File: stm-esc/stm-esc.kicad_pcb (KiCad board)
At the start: 2 copper layers, 57 x 48 mm, 39 parts, among them J1 RCP, J10 COUT, J2 Conn_01x06, J3 USART, J4 Conn_01x06, J5 SWIM, J6 AOUT, J7 CONN_01X01, J8 CONN_01X01, J9 BOUT, Q1 FDMS86350, Q2 FDMS86350, Q3 FDMS86350, Q4 FDMS86350, Q5 FDMS86350, Q6 FDMS86350, U2 APE8865N-33-HF-3, U3 stm32f051xx-lqfp32, U4 IR2103, U5 IR2103, U6 IR2103

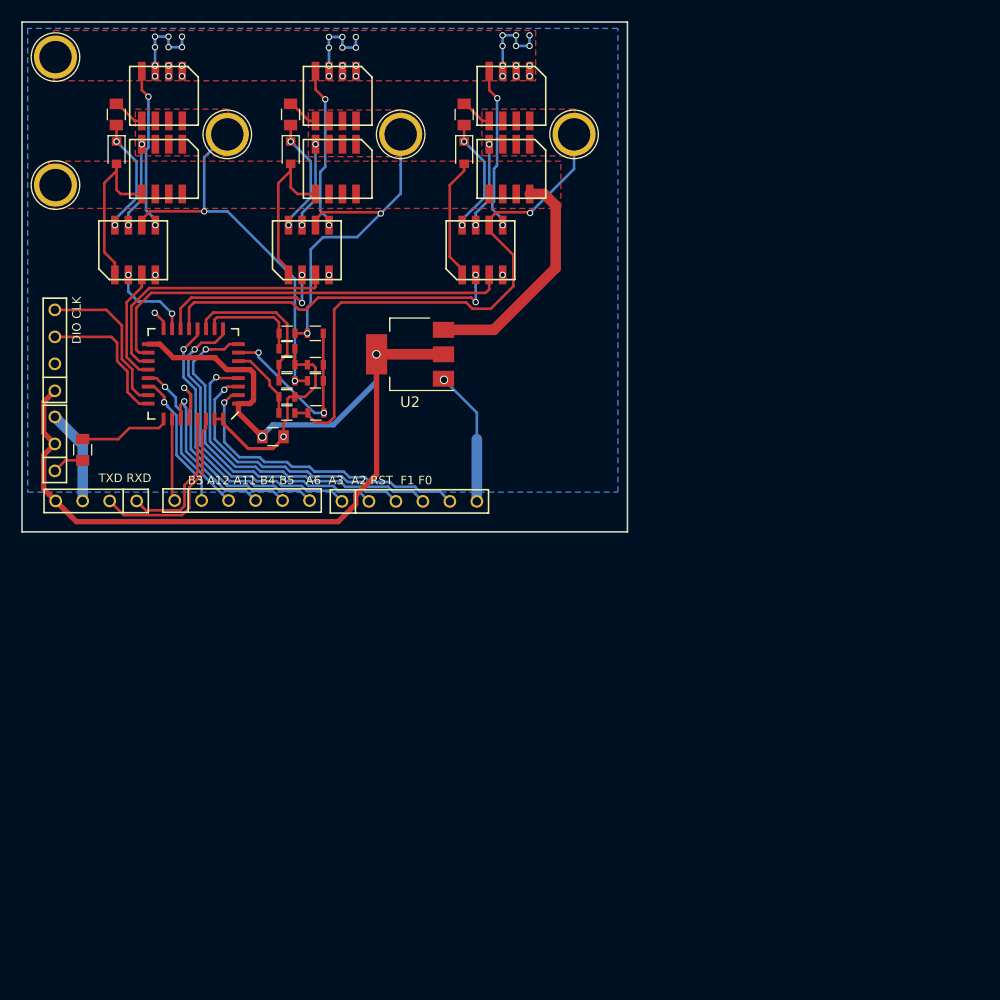
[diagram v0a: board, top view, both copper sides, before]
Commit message: stm-esc 48pin mcu 定板打样
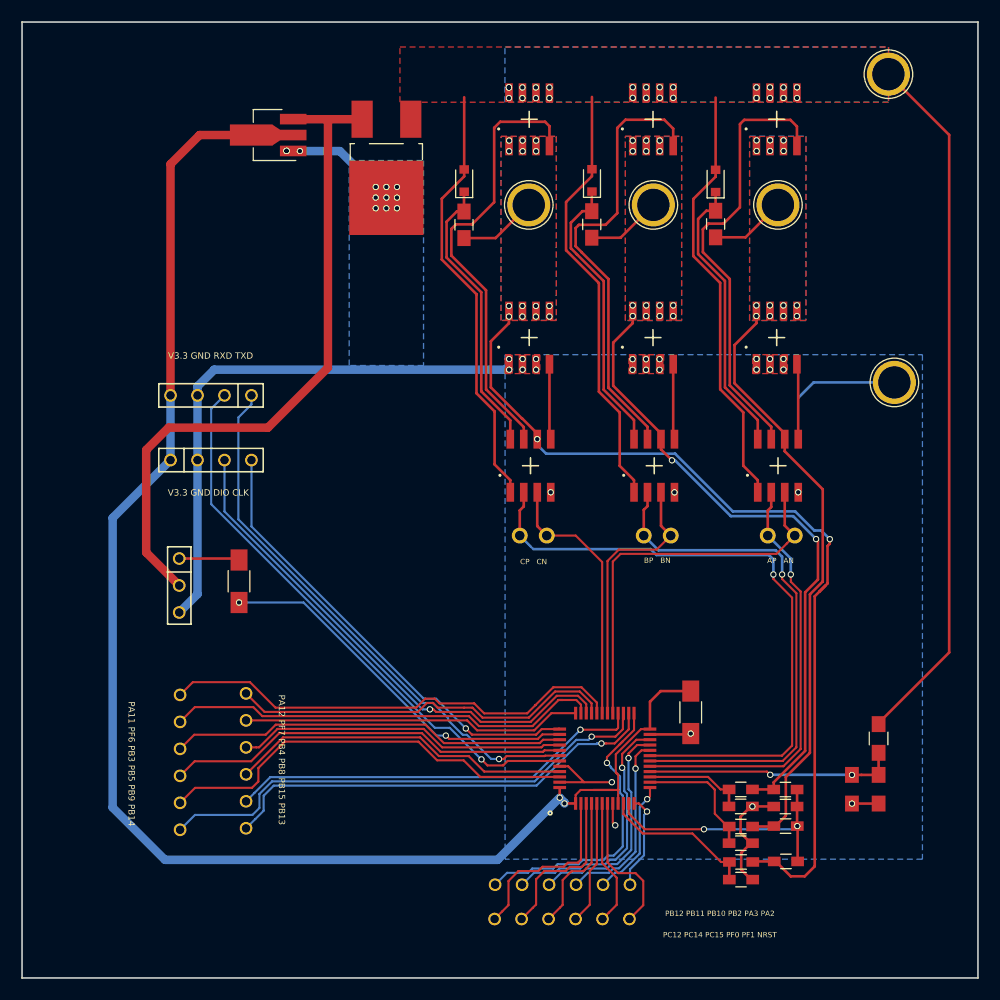
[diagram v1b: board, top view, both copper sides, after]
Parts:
- removed J2: Conn_01x06, my_footprint:conn-6x2.54mm
- removed the R2 at (44.9, 50.8)
- added J11: AOUT, Connectors:1pin, F.Cu at (91.2, 37.2)
- added J12: Conn_01x02, my_footprint:SIP-2xP2.54mm, F.Cu at (79.8, 68.3)
- added J13: CONN_01X01, Connectors:1pin, F.Cu at (101.6, 24.9)
- added J14: CONN_01X01, Connectors:1pin, F.Cu at (102.1, 53.9)
- added J15: BOUT, Connectors:1pin, F.Cu at (79.4, 37.2)
- added J16: COUT, Connectors:1pin, F.Cu at (67.7, 37.2)
- added R11: 20K, Resistors_SMD:R_0603_HandSoldering, F.Cu at (91.9, 92.3)
- added R12: 20K, Resistors_SMD:R_0603_HandSoldering, F.Cu at (91.9, 95.7)
- added R2: R, Resistors_SMD:R_0805_HandSoldering, F.Cu at (98.1, 92.2)
- added R2: R, Resistors_SMD:R_0805_HandSoldering, F.Cu at (100.6, 92.2)
- added U1: L7805, TO_SOT_Packages_SMD:TO-252-2_Rectifier, F.Cu at (54.3, 33.7)
- C1, C2: footprint Capacitors_SMD:C_0805 -> Capacitors_SMD:C_1206_HandSoldering
- C3, C4, C5: footprint Capacitors_SMD:C_0805 -> Capacitors_SMD:C_0805_HandSoldering
- J1: value RCP -> Conn_01x06; footprint my_footprint:conn-3x2.54mm -> my_footprint:conn-6x2.54mm
- J10: value COUT -> Conn_01x02; footprint Connectors:1pin -> my_footprint:SIP-2xP2.54mm
- J3: value USART -> Conn_01x06; footprint my_footprint:conn-4x2.45mm -> my_footprint:conn-6x2.54mm
- J4: value Conn_01x06 -> Conn_01x03; footprint my_footprint:conn-6x2.54mm -> my_footprint:conn-3x2.54mm
- J5: value SWIM -> Conn_01x02; footprint my_footprint:conn-4x2.45mm -> my_footprint:SIP-2xP2.54mm
- J6: value AOUT -> Conn_01x06; footprint Connectors:1pin -> my_footprint:conn-6x2.54mm
- J7, J8: value CONN_01X01 -> Conn_01x04; footprint Connectors:1pin -> my_footprint:conn-4x2.54mm
- J9: value BOUT -> Conn_01x06; footprint Connectors:1pin -> my_footprint:conn-6x2.54mm
- R1: value 3K -> R; footprint Resistors_SMD:R_0603 -> Resistors_SMD:R_0805_HandSoldering
- R10, R3, R7, R9: footprint Resistors_SMD:R_0603 -> Resistors_SMD:R_0603_HandSoldering
- R4, R5: value 20K -> 3K; footprint Resistors_SMD:R_0603 -> Resistors_SMD:R_0603_HandSoldering
- R6: value 20K -> 1K; footprint Resistors_SMD:R_0603 -> Resistors_SMD:R_0603_HandSoldering
- R8: value 1K -> 20K; footprint Resistors_SMD:R_0603 -> Resistors_SMD:R_0603_HandSoldering
- U2: footprint TO_SOT_Packages_SMD:SOT-223-3_TabPin2 -> TO_SOT_Packages_SMD:SOT-89-3_Handsoldering
- U3: value stm32f051xx-lqfp32 -> STM32F0XX-QFP48; footprint my_footprint:LQFP_32 -> my_footprint:QFP_48_P0.5_W0.3
- moved J6 66.6 mm to (41.1, 89.6), turned to 90 degrees
- moved R3 64.6 mm to (87.7, 100.7)
- moved J10 64.4 mm to (91.5, 68.3), turned to 0 degrees
- moved R1 64.3 mm to (100.6, 87.5), turned to 90 degrees
- moved R5 64.3 mm to (87.7, 97.3), turned to 180 degrees
- moved J1 63.3 mm to (70.9, 101.2), turned to 0 degrees
- moved J9 62.7 mm to (34.9, 89.7), turned to 90 degrees
- moved C1 62.4 mm to (83.0, 85.0)
- moved R9 61.3 mm to (87.7, 95.7)
- moved R10 61.2 mm to (91.9, 99.0), turned to 180 degrees
- moved R7 60.5 mm to (87.7, 99.1)
- moved R6 59.8 mm to (91.9, 93.9)
- moved J3 58.9 mm to (70.8, 104.5)
- moved R4 58.6 mm to (87.7, 93.8), turned to 180 degrees
- moved R8 56.6 mm to (87.7, 92.2)
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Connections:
- C1 pad 1: /RCP -> +3V3
- C1 pad 2: Net-(C1-Pad2) -> GND
- C2 pad 1: +3V3 -> /RCP
- C2 pad 2: GND -> Net-(C2-Pad2)
- J1 pad 1: Net-(C1-Pad2) -> /PB12
- J1 pad 2: +3V3 -> /PB11
- J1 pad 3: GND -> /PB10
- J10 pad 1: COUT -> AP
- J3 pad 1: /TXD -> /NRST
- J3 pad 2: /RXD -> /PF1
- J3 pad 3: GND -> /PF0
- J3 pad 4: +3V3 -> /PC15
- J4 pad 1: /PA3 -> Net-(C2-Pad2)
- J4 pad 2: /PA2 -> +5V
- J4 pad 3: /NRST -> GND
- J5 pad 1: +3V3 -> CP
- J5 pad 2: GND -> CN
- J6 pad 1: AOUT -> PB13
- J7 pad 1: VCC -> /TXD
- J8 pad 1: GND -> +3V3
- J9 pad 1: BOUT -> PB14
- R1 pad 1: GND -> /Vsample
- R1 pad 2: /FA+ -> VCC
- R10 pad 1: AOUT -> Fabc
- R10 pad 2: /Fabc- -> COUT
- R3 pad 2: /FC+ -> Fc
- R4 pad 1: /FC+ -> GND
- R4 pad 2: COUT -> Fb
- R5 pad 1: /FB+ -> GND
- R5 pad 2: BOUT -> Fa
- R6 pad 1: /FA+ -> GND
- R6 pad 2: AOUT -> Fabc
- R7 pad 1: COUT -> Fc
- R7 pad 2: /Fabc- -> COUT
- R8 pad 1: GND -> Fb
- R8 pad 2: /Fabc- -> BOUT
- R9 pad 1: BOUT -> Fa
- R9 pad 2: /Fabc- -> AOUT
- U2 pad 3: VCC -> +5V
- U3 pad 10: /FB+ -> Fc
- U3 pad 11: /FC+ -> Fabc
- U3 pad 12: /PA6 -> /PA2
- U3 pad 13: AP -> /PA3
- U3 pad 14: BP -> Fa
- U3 pad 15: CP -> Fb
- U3 pad 16: GND -> /Vsample
- U3 pad 17: +3V3 -> AP
- U3 pad 18: AN -> BP
- U3 pad 19: BN -> CP
- U3 pad 2: /PF0 -> /PC13
- U3 pad 20: CN -> /PB2
- U3 pad 21: /PA11 -> /PB10
- U3 pad 22: /PA12 -> /PB11
- U3 pad 23: /SWCLK -> GND
- U3 pad 24: /SWDIO -> +3V3
- U3 pad 25: /RCP -> /PB12
- U3 pad 26: /PB3 -> PB13
- U3 pad 27: /PB4 -> PB14
- U3 pad 28: /PB5 -> PB15
- U3 pad 29: /TXD -> AN
- U3 pad 3: /PF1 -> /PC14
- U3 pad 30: /RXD -> BN
- U3 pad 31: GND -> CN
- U3 pad 32: GND -> PA11
- U3 pad 4: /NRST -> /PC15
- U3 pad 5: +3V3 -> /PF0
- U3 pad 6: /FA+ -> /PF1
- U3 pad 7: /Fabc- -> /NRST
- U3 pad 8: /PA2 -> GND
- U3 pad 9: /PA3 -> +3V3
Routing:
- net VCC: track 65.7 -> 188.5 mm, vias 0 -> 25
- net +5V: track 0.00 -> 64.3 mm
- net CP: track 7.98 -> 62.6 mm, vias 2 -> 1
- net COUT: track 40.4 -> 93.3 mm, vias 2 -> 16
- net PB14: track 0.00 -> 47.9 mm, vias 0 -> 1
- net +3V3: track 98.0 -> 144.6 mm
- net PA11: track 0.00 -> 44.3 mm
- net /SWDCLK: track 0.00 -> 43.7 mm, vias 0 -> 1
- net PB13: track 0.00 -> 42.2 mm, vias 0 -> 1
- net PF6: track 0.00 -> 41.4 mm
- net PB9: track 0.00 -> 40.2 mm
- net PB15: track 0.00 -> 39.3 mm, vias 0 -> 1
- net /TXD: track 13.7 -> 52.0 mm, vias 0 -> 1
- net PB5: track 0.00 -> 38.2 mm
- net PB3: track 0.00 -> 37.5 mm
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- added copper zone on B.Cu, net AOUT
- added copper zone on B.Cu, net BOUT
- added copper zone on B.Cu, net COUT
- added copper zone on B.Cu, net VCC
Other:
- board size 57 x 48 mm -> 90 x 90 mm
- board text added: "AP AN"
- board text added: "BP BN"
- board text added: "CP CN"
- board text added: "PA11 PF6 PB3 PB5 PB9 PB14"
- board text added: "PA12 PF7 PB4 PB8 PB15 PB13"
- board text added: "PB12 PB11 PB10 PB2 PA3 PA2"
- board text added: "PC12 PC14 PC15 PF0 PF1 NRST"
- board text added: "V3.3 GND DIO CLK"
- board text added: "V3.3 GND RXD TXD"
- board text removed: "B3 A12 A11 B4 B5 A6 A3 A2 RST F1 F0"
- board text removed: "DIO CLK"
- board text removed: "TXD RXD"

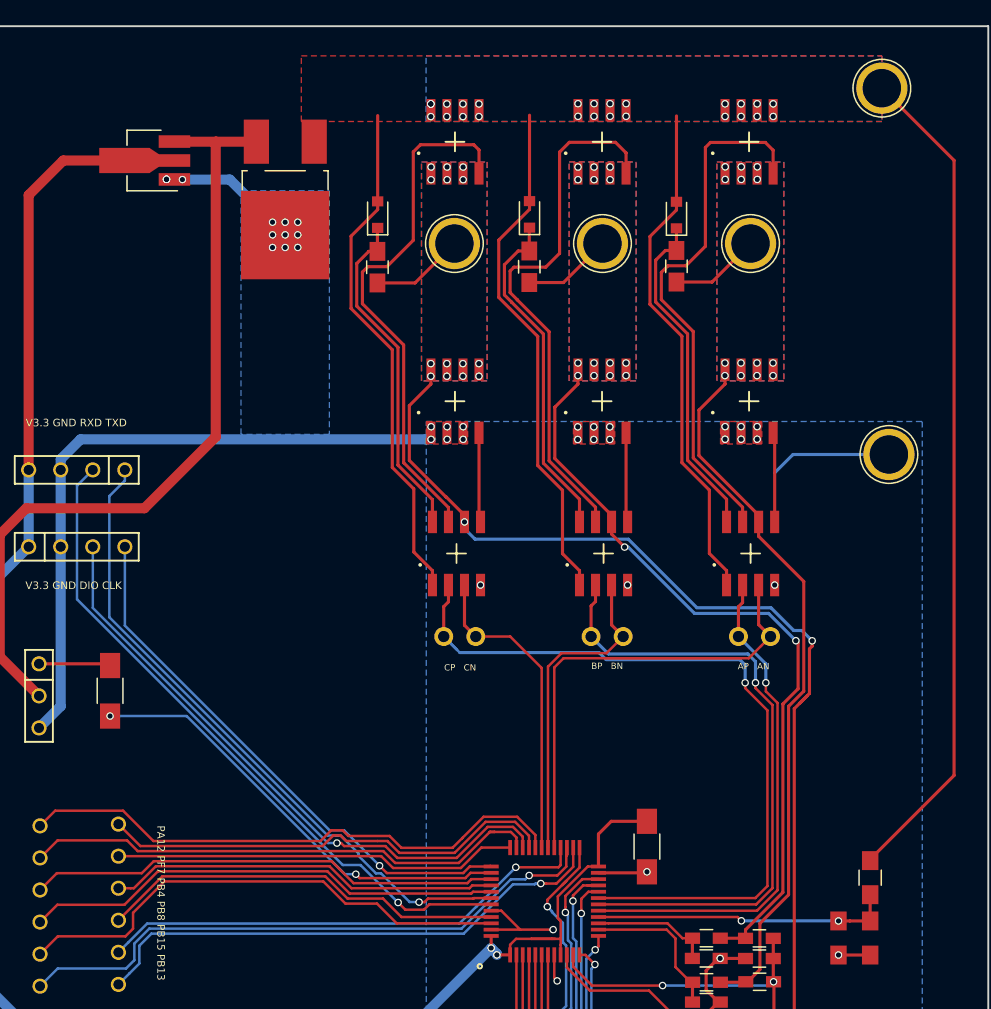
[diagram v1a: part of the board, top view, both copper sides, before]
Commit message: minor change for stm-esc
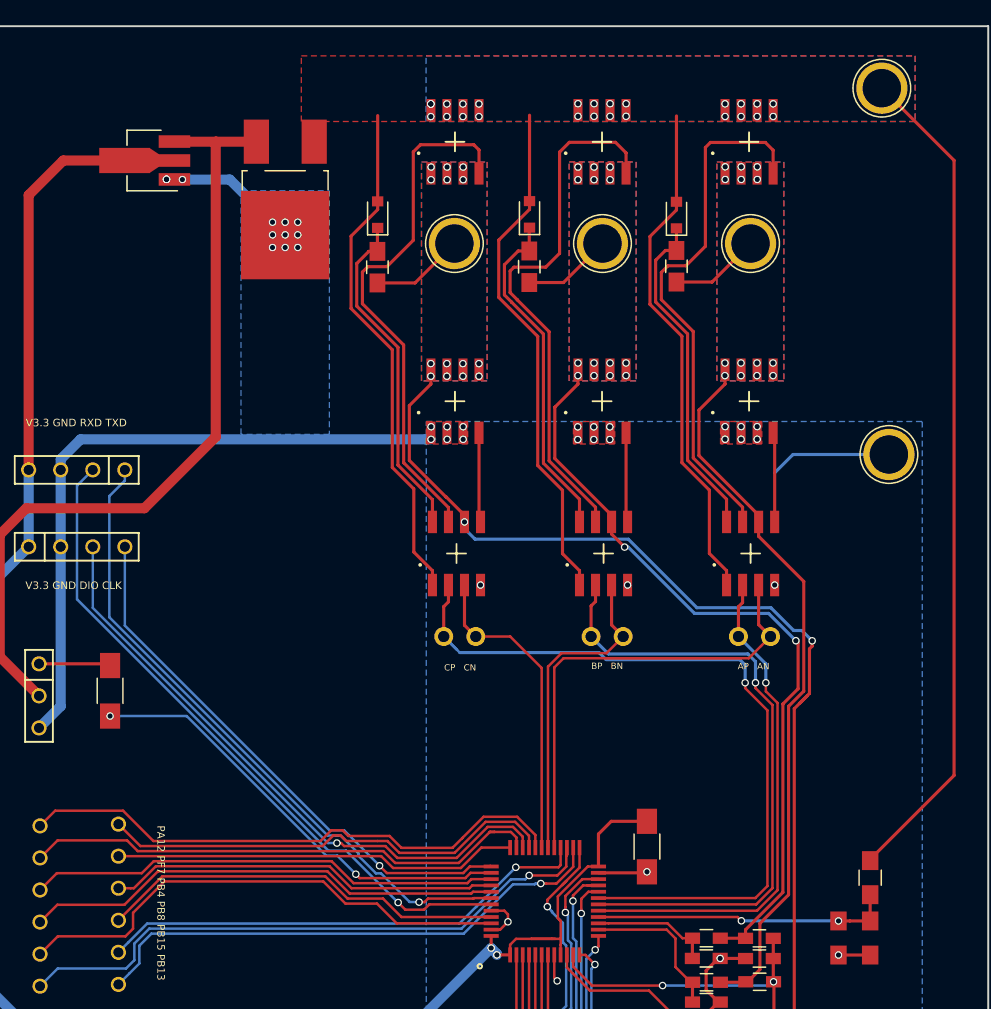
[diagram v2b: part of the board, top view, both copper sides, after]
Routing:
- net GND: track 101.6 -> 97.4 mm
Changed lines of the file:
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@@
   (general
     (links 159)
-    (no_connects 6)
+    (no_connects 4)
     (area 19.924999 19.924999 110.075001 110.075001)
     (thickness 1.6)
     (drawings 13)
-    (tracks 795)
+    (tracks 799)
     (zones 0)
     (modules 48)
@@
   (gr_line (start 20 20) (end 20 110) (layer Edge.Cuts) (width 0.15))
   (gr_line (start 20 20) (end 110 20) (layer Edge.Cuts) (width 0.15))
+  (segment (start 71.95 90.36) (end 71.95 90.95) (width 0.2) (layer F.Cu) (net 1))
+  (segment (start 70.62 91.57) (end 71.33 91.57) (width 0.2) (layer F.Cu) (net 1))
+  (segment (start 71.33 91.57) (end 71.95 90.95) (width 0.2) (layer F.Cu) (net 1))
+  (segment (start 71.66 90.07) (end 71.95 90.36) (width 0.2) (layer F.Cu) (net 1))
+  (segment (start 70.62 90.07) (end 71.66 90.07) (width 0.2) (layer F.Cu) (net 1))
   (via (at 98.13436 93.582096) (size 0.6) (drill 0.4) (layers F.Cu B.Cu) (net 1))
   (segment (start 98.13436 93.582096) (end 100.64436 93.582096) (width 0.25) (layer F.Cu) (net 1))
@@
   (segment (start 38.091472 52.73) (end 65.435736 52.73) (width 0.8) (layer B.Cu) (net 1))
   (segment (start 36.52 55.15) (end 36.52 61.24) (width 0.8) (layer B.Cu) (net 1))
-  (segment (start 70.62 91.57) (end 75.53 91.57) (width 0.2) (layer F.Cu) (net 1))
-  (segment (start 71.42 90.07) (end 72.92 91.57) (width 0.2) (layer F.Cu) (net 1))
-  (segment (start 70.62 90.07) (end 71.42 90.07) (width 0.2) (layer F.Cu) (net 1))
   (segment (start 75.62 93.57) (end 75.62 95.4) (width 0.2) (layer F.Cu) (net 1))
   (segment (start 75.62 95.4) (end 75.85 95.63) (width 0.2) (layer F.Cu) (net 1))
   (via (at 75.85 95.63) (size 0.6) (drill 0.4) (layers F.Cu B.Cu) (net 1))
-  (via (at 75.53 91.57) (size 0.6) (drill 0.4) (layers F.Cu B.Cu) (net 1))
+  (via (at 71.95 90.95) (size 0.6) (drill 0.4) (layers F.Cu B.Cu) (net 1))
   (via (at 82.96 86.99) (size 0.6) (drill 0.4) (layers F.Cu B.Cu) (net 1))
   (via (at 88.76 93.85) (size 0.6) (drill 0.4) (layers F.Cu B.Cu) (net 1))
@@
   (segment (start 80.13 82.99) (end 82.96 82.99) (width 0.25) (layer F.Cu) (net 2))
   (segment (start 79.12 86.57) (end 79.12 84) (width 0.25) (layer F.Cu) (net 2))
+  (segment (start 40.43 74.65) (end 46.5 74.65) (width 0.2) (layer B.Cu) (net 3))
+  (segment (start 46.5 74.65) (end 57.56001 85.710011) (width 0.2) (layer B.Cu) (net 3))
+  (segment (start 58.440011 85.720011) (end 59.9 87.18) (width 0.2) (layer B.Cu) (net 3))
+  (segment (start 57.56001 85.710011) (end 58.440011 85.710011) (width 0.2) (layer B.Cu) (net 3))
+  (segment (start 58.440011 85.710011) (end 58.440011 85.720011) (width 0.2) (layer B.Cu) (net 3))
   (segment (start 68.568621 87.48998) (end 60.20998 87.48998) (width 0.2) (layer F.Cu) (net 3))
   (segment (start 60.20998 87.48998) (end 59.9 87.18) (width 0.2) (layer F.Cu) (net 3))
-  (segment (start 59.03 87.18) (end 59.9 87.18) (width 0.2) (layer B.Cu) (net 3))
   (segment (start 70.62 87.07) (end 68.988601 87.07) (width 0.2) (layer F.Cu) (net 3))
   (segment (start 68.988601 87.07) (end 68.568621 87.48998) (width 0.2) (layer F.Cu) (net 3))
-  (segment (start 40.43 74.65) (end 46.5 74.65) (width 0.2) (layer B.Cu) (net 3))
-  (segment (start 46.5 74.65) (end 59.03 87.18) (width 0.2) (layer B.Cu) (net 3))
   (via (at 59.9 87.18) (size 0.6) (drill 0.4) (layers F.Cu B.Cu) (net 3))
   (via (at 40.43 74.65) (size 0.6) (drill 0.4) (layers F.Cu B.Cu) (net 3))
@@
   (segment (start 65.334264 89.39) (end 65.614254 89.11001) (width 0.2) (layer F.Cu) (net 15))
   (via (at 64.91 89.39) (size 0.6) (drill 0.4) (layers F.Cu B.Cu) (net 15))
-  (segment (start 63.25 89.42) (end 63.2363 89.42) (width 0.2) (layer B.Cu) (net 16))
-  (segment (start 37.81 65.394302) (end 37.81 56.4) (width 0.2) (layer B.Cu) (net 16))
-  (segment (start 63.2363 89.42) (end 60.268451 86.452151) (width 0.2) (layer B.Cu) (net 16))
-  (segment (start 60.268451 86.452151) (end 58.867849 86.452151) (width 0.2) (layer B.Cu) (net 16))
-  (segment (start 58.867849 86.452151) (end 37.81 65.394302) (width 0.2) (layer B.Cu) (net 16))
-  (segment (start 37.81 56.4) (end 39.06 55.15) (width 0.2) (layer B.Cu) (net 16))
+  (segment (start 39.06 55.15) (end 37.81 56.4) (width 0.2) (layer B.Cu) (net 16))
+  (segment (start 37.81 56.4) (end 37.81 65.394302) (width 0.2) (layer B.Cu) (net 16))
+  (segment (start 37.81 65.394302) (end 57.725699 85.310001) (width 0.2) (layer B.Cu) (net 16))
+  (segment (start 57.725699 85.310001) (end 59.126301 85.310001) (width 0.2) (layer B.Cu) (net 16))
+  (segment (start 59.126301 85.310001) (end 63.2363 89.42) (width 0.2) (layer B.Cu) (net 16))
+  (segment (start 63.2363 89.42) (end 63.25 89.42) (width 0.2) (layer B.Cu) (net 16))
   (segment (start 63.25 89.42) (end 63.820001 89.990001) (width 0.2) (layer F.Cu) (net 16))
   (segment (start 63.820001 89.990001) (end 65.299962 89.990001) (width 0.2) (layer F.Cu) (net 16))
@@
     (polygon
       (pts
-        (xy 65.46 22.35) (xy 101.58 22.35) (xy 101.58 27.55) (xy 65.46 27.55)
+        (xy 65.46 22.35) (xy 104.21 22.35) (xy 104.21 27.55) (xy 65.46 27.55)
       )
     )
@@
     (polygon
       (pts
-        (xy 55.579313 22.35) (xy 101.58 22.35) (xy 101.58 27.55) (xy 55.579313 27.55)
+        (xy 55.579313 22.35) (xy 104.21 22.35) (xy 104.21 27.55) (xy 55.579313 27.55)
       )
     )
